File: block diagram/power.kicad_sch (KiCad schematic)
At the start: 4 parts

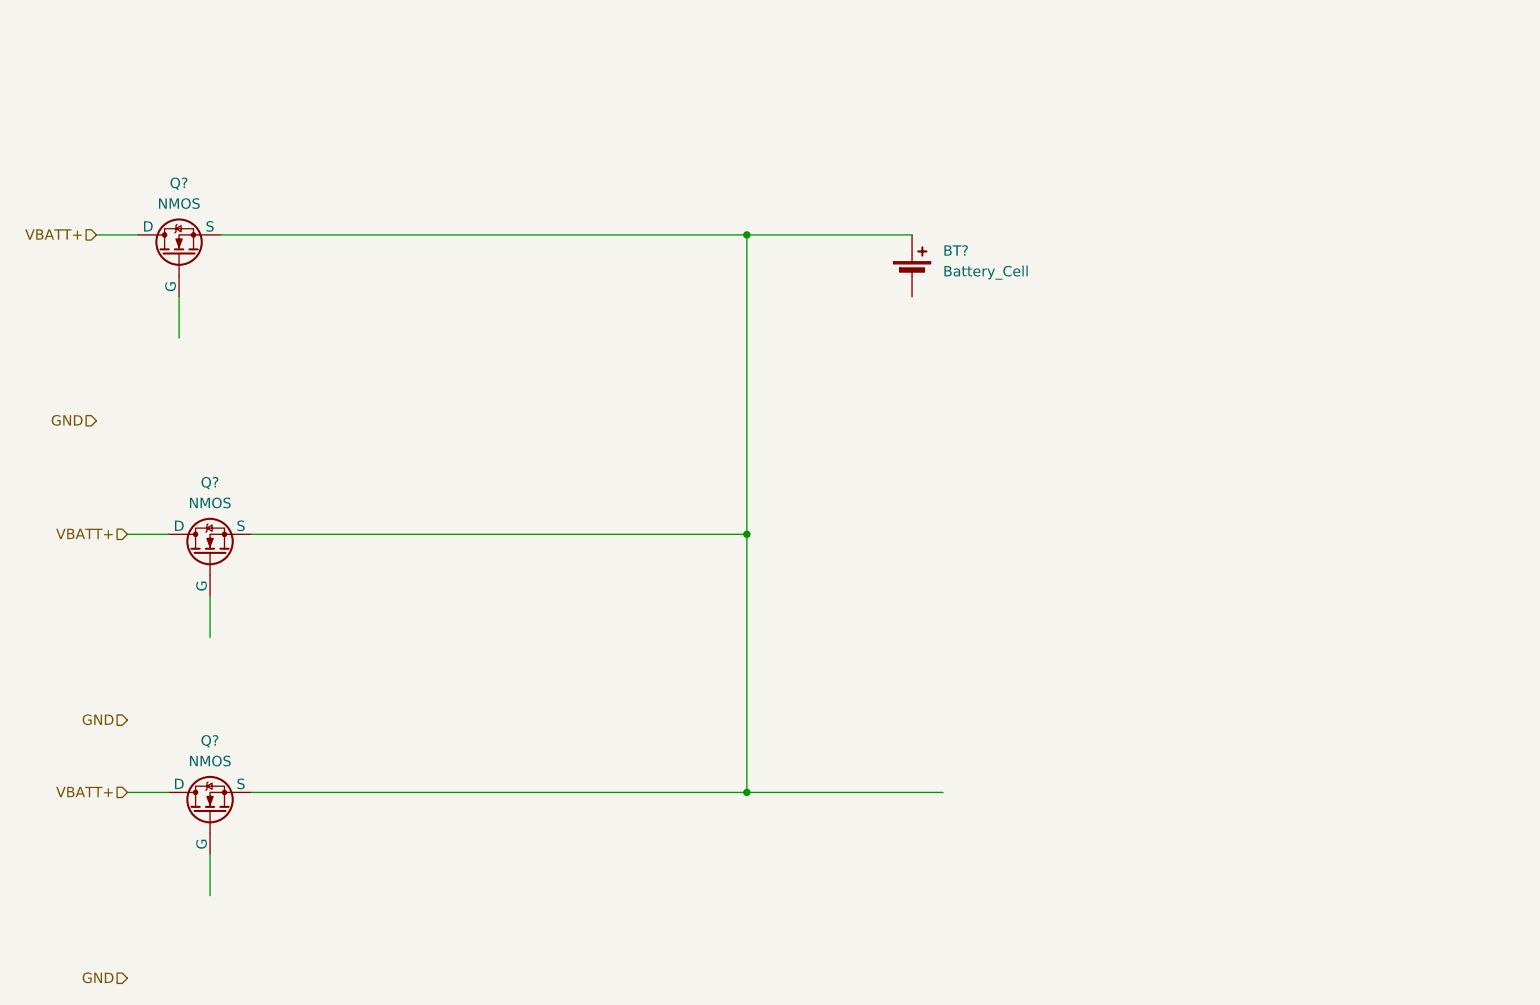
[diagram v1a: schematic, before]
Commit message: battery spec added
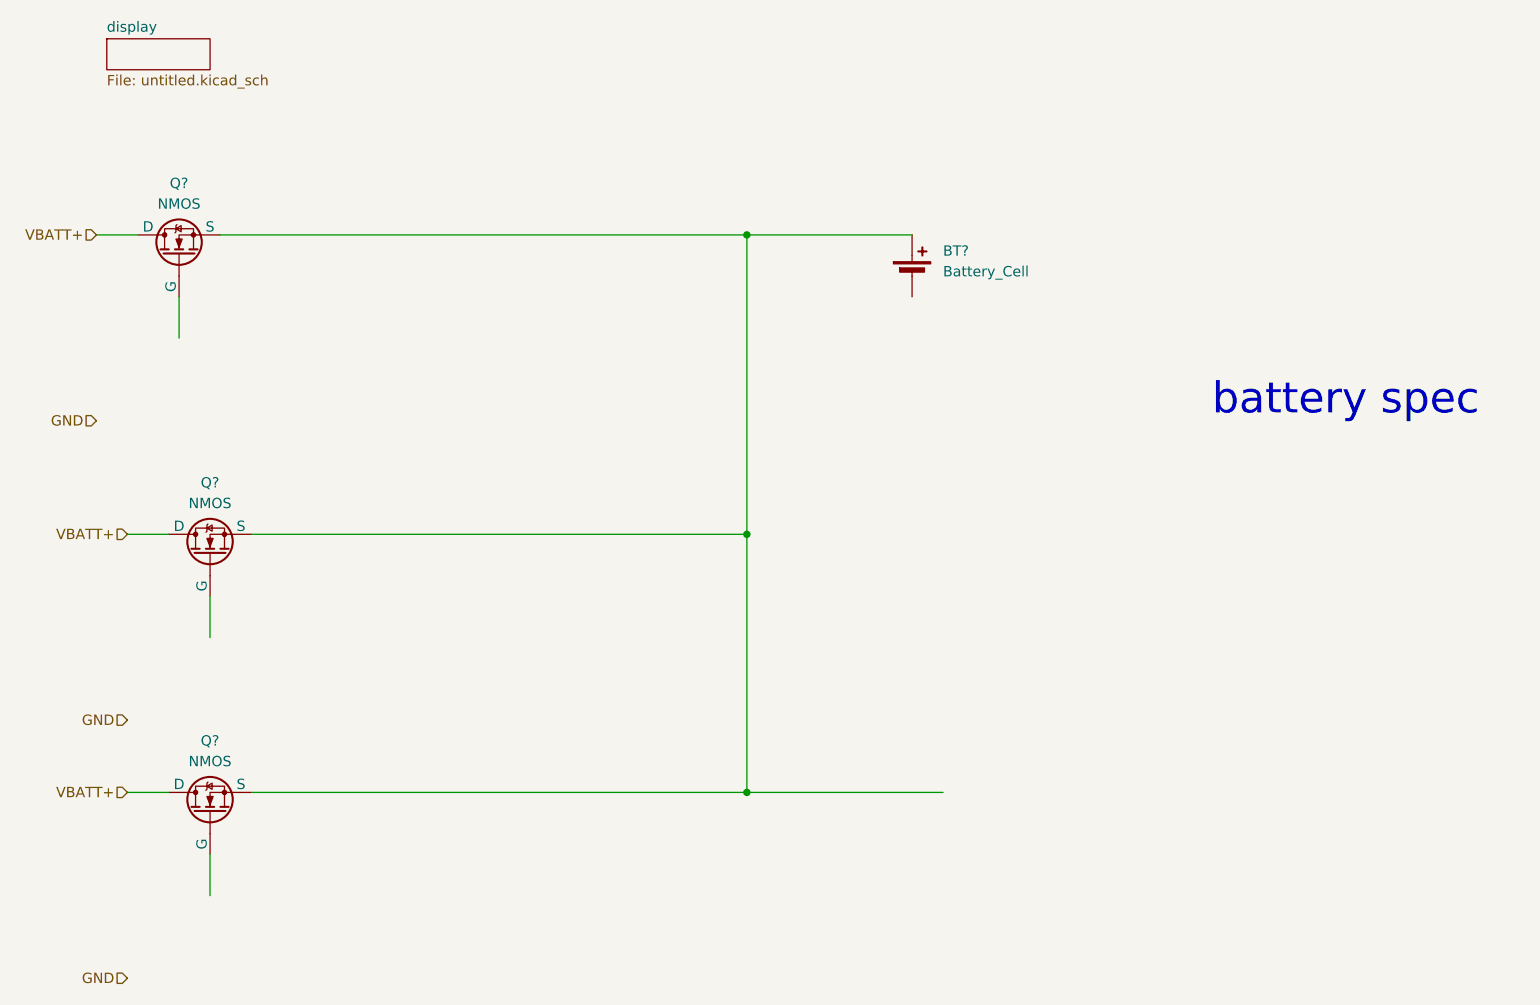
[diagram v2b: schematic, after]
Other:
- added sheet display (untitled.kicad_sch)
- note added: "battery spec"
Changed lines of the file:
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@@
 	(generator_version "9.0")
 	(paper "A4")
+	(text "battery spec"
+		(exclude_from_sim no)
+		(at 254 83.82 0)
+		(effects
+			(font
+				(size 3.81 3.81)
+			)
+			(href "https://www.alibaba.com/product-detail/XINGTO-Wholesale-OEM-ODM-XT60-Plug_1601588295564.html?spm=a2700.prosearch.normal_offer.d_title.105567afqntwCz&priceId=958610057aa24b5f973c01c3b15eb7c2")
+		)
+	)
 	(junction
 		(at 180.34 132.08)
@@
 				)
 			)
+		)
+	)
+	(sheet
+		(at 101.6 39.37)
+		(size 12.7 3.81)
+		(exclude_from_sim no)
+		(in_bom yes)
+		(on_board yes)
+		(dnp no)
+		(fields_autoplaced yes)
+		(stroke
+			(width 0.1524)
+			(type solid)
+			(color 132 0 0 1)
+		)
+		(fill
+			(color 255 255 194 1.0000)
+		)
+		(property "Sheetname" "display"
+			(at 101.6 38.6584 0)
+			(effects
+				(font
+					(size 1.27 1.27)
+				)
+				(justify left bottom)
+			)
+		)
+		(property "Sheetfile" "untitled.kicad_sch"
+			(at 101.6 43.7646 0)
+			(effects
+				(font
+					(size 1.27 1.27)
+				)
+				(justify left top)
+			)
+		)
+		(property "Field2" ""
+			(at 101.6 39.37 0)
+			(effects
+				(font
+					(size 1.27 1.27)
+				)
+			)
+		)
+		(instances
+			(project "block diagram"
+				(path "/77b537aa-abd1-4b45-8666-f13206102f09/a1f87f20-3215-4349-bfe0-f2b04b01f16e"
+					(page "13")
+				)
+			)

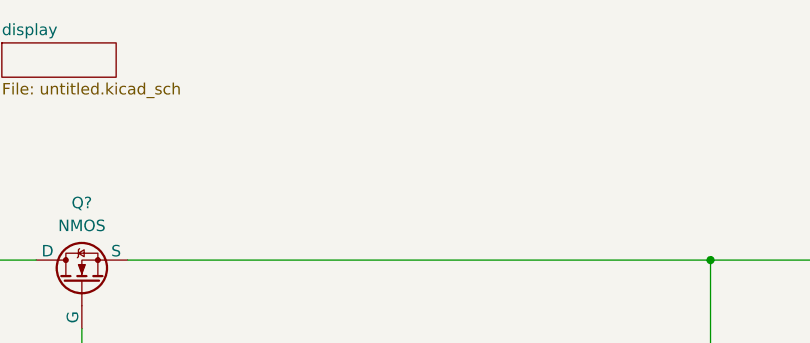
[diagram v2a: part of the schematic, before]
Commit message: diagrammed bt chip, please fix formatting
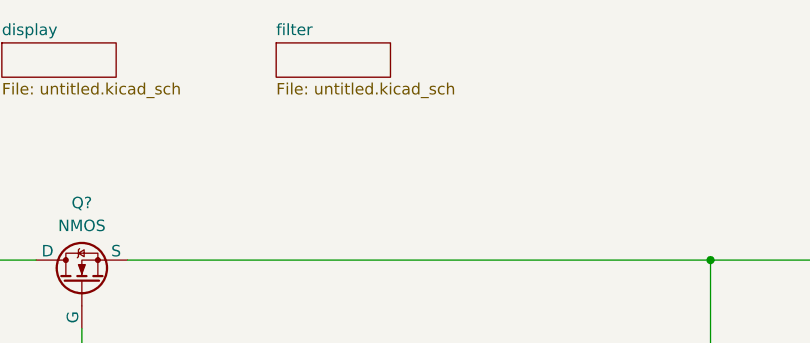
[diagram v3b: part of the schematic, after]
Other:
- added sheet filter (untitled.kicad_sch)
